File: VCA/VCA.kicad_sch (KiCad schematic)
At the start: 6 parts, among them J1 AudioJack2_SwitchT, J2 AudioJack2_SwitchT, J3 AudioJack2_SwitchT, U1 TLP175A, U2 TLP175A

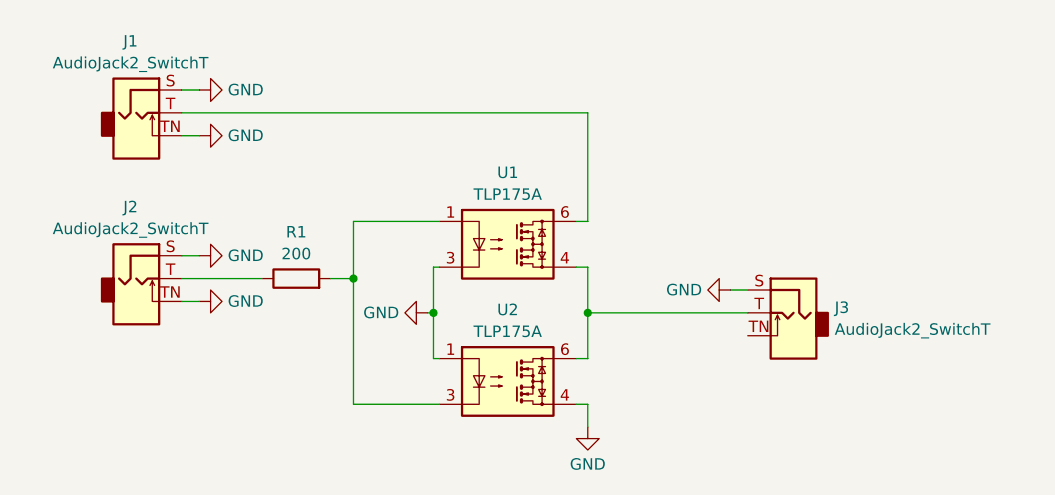
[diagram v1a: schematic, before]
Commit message: Add VCA layout
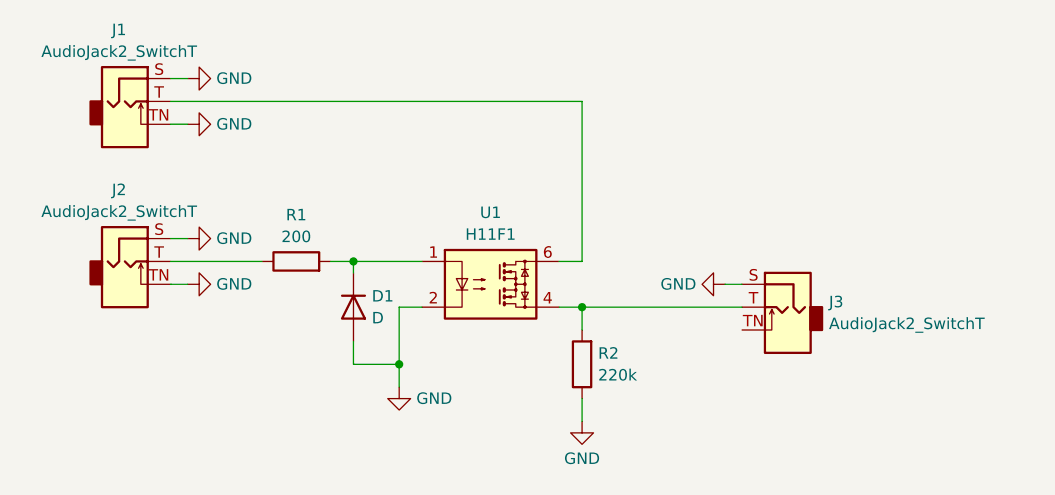
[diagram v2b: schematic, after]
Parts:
- removed U1, U2: TLP175A, Package_SO:MFSOP6-4_4.4x3.6mm_P1.27mm, symbol Relay_SolidState:TLP175A
- added D1: D, Diode_SMD:D_SOD-323_HandSoldering, symbol Device:D
- added R2: 220k, Resistor_SMD:R_0603_1608Metric, symbol Device:R
- added U1: H11F1, Package_DIP:DIP-6_W8.89mm_SMDSocket_LongPads, symbol Relay_SolidState:TLP3542
- J1, J2, J3: footprint (none) -> Custom_FP:PJ398SM
- R1: footprint (none) -> Resistor_SMD:R_0603_1608Metric
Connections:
- net GND: now also D1.2 (A), R2.1, U1.2
- net at J1.T: now also U1.6
- net at R1.2: now also D1.1 (K), U1.1
- net at J3.T: now also R2.2, U1.4
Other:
- moved on the sheet: J1, J2, J3, R1
